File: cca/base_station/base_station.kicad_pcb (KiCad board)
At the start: 2 copper layers, 76.2 x 50.8 mm, 11 parts, among them P1 tstat_ui_conn, P2 tstat_cable_con, U1 RFM69W, U2 DHT22, U3 TEENSY-LC

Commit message: 0.5mm fab pass
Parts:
- moved AE1 6.54 mm to (34.5, 52.9)
- moved P2 2.54 mm to (88.1, 35.6)
- moved U1 2.54 mm to (56.1, 62.3)
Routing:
- net Net-(AE1-Pad1): track 7.89 -> 3.89 mm
- net +3V3: track 122.1 -> 126.0 mm, vias 3 -> 2
- net Net-(U1-Pad2): track 44.3 -> 47.9 mm
- net Net-(P2-Pad7): track 13.4 -> 10.9 mm
- net Net-(P2-Pad6): track 13.5 -> 10.9 mm
- net Net-(P2-Pad5): track 13.5 -> 10.9 mm
- net Net-(P2-Pad4): track 13.5 -> 10.9 mm
- net Net-(P2-Pad8): track 13.4 -> 11.0 mm
- net Net-(U1-Pad15): track 41.0 -> 39.0 mm
- net GND: track 24.1 -> 25.6 mm
- net Net-(P1-Pad5): track 21.1 -> 19.6 mm
- net Net-(P1-Pad3): track 19.1 -> 20.5 mm
- net Net-(U1-Pad13): track 35.3 -> 34.4 mm
- net Net-(U1-Pad14): track 38.0 -> 37.3 mm
- net +5V: track 78.1 -> 77.6 mm
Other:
- net class 3.3v: clearance 0.2 -> 0.51; via_dia 1.1 -> 1.5
- net class 5v: clearance 0.4 -> 0.51; via_dia 1.1 -> 1.5
- net class Default: clearance 0.4 -> 0.51; trace_width 0.25 -> 0.5; via_dia 1.1 -> 1.5
- net class ant: clearance 0.4 -> 0.51; via_dia 1.1 -> 1.5
- net class gnd: clearance 0.2 -> 0.51; via_dia 1.1 -> 1.5
- rule trace_clearance: 0.4 -> 0.51
- rule trace_min: 0.2 -> 0.5

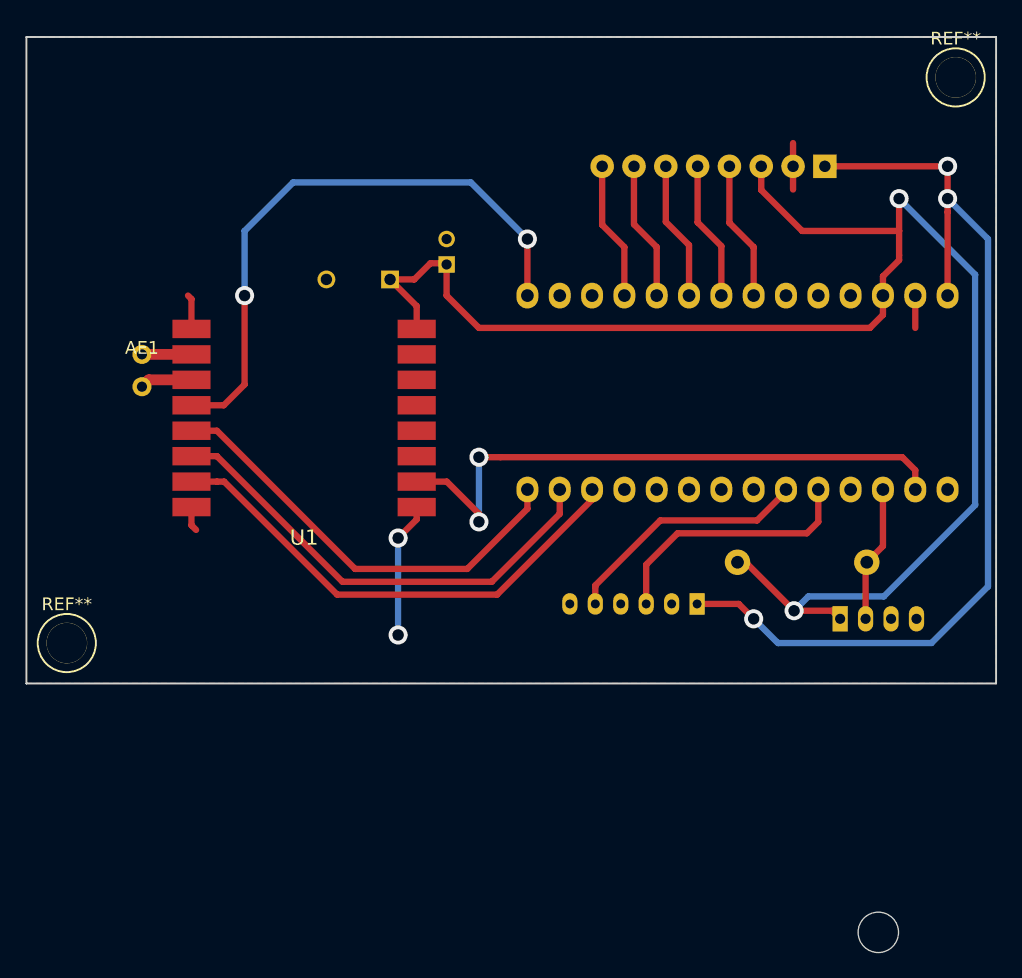
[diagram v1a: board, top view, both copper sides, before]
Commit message: updated wire holes and antenna to be 1.0mm drill. Added missing 3.3V optional e-point
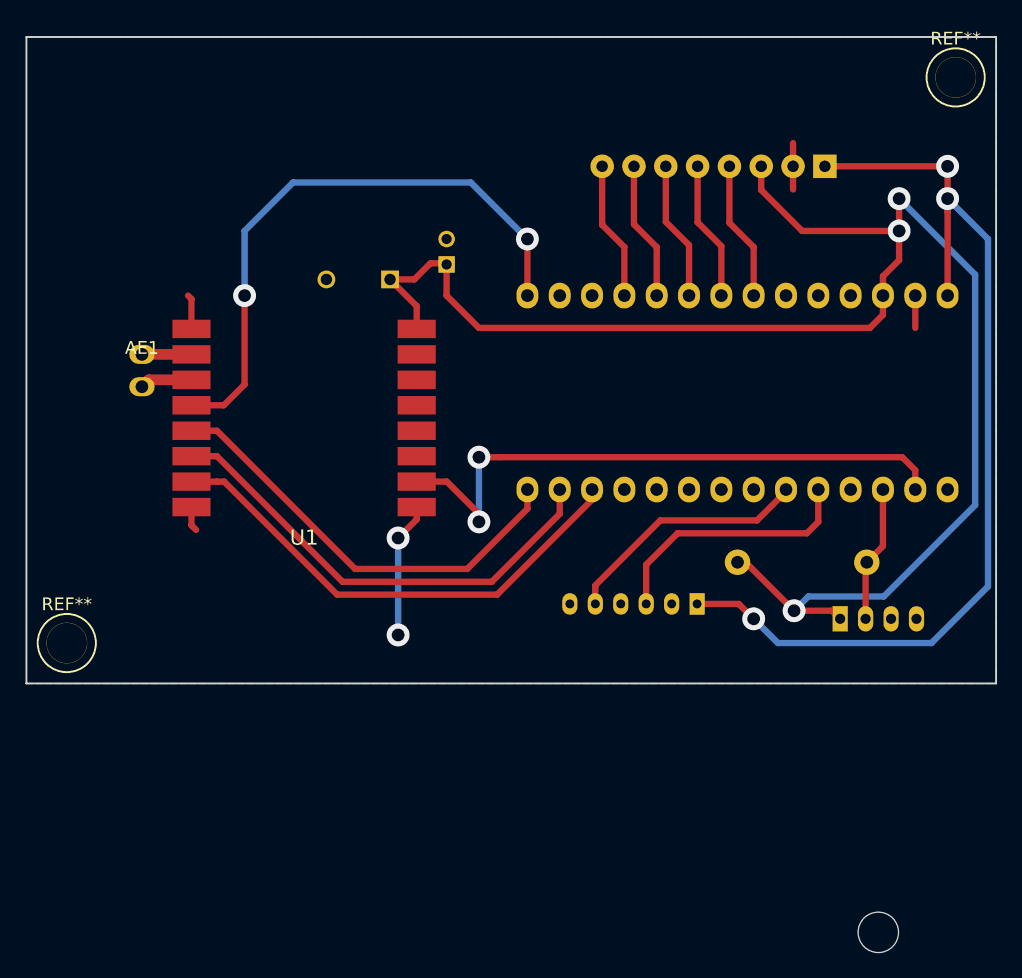
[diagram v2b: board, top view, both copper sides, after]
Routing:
- net +3V3: vias 2 -> 3
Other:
- net class 3.3v: via_dia 1.5 -> 1.8; via_drill 0.9 -> 1
- net class 5v: via_dia 1.5 -> 1.8; via_drill 0.9 -> 1
- net class Default: via_dia 1.5 -> 1.8; via_drill 0.9 -> 1
- net class ant: via_dia 1.5 -> 1.8; via_drill 0.9 -> 1
- net class gnd: via_dia 1.5 -> 1.8; via_drill 0.9 -> 1
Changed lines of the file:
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@@
     (links 36)
     (no_connects 0)
-    (area 25.324999 24.242 102.115 98.883001)
+    (area 25.324999 25.324999 101.675001 76.275001)
     (thickness 1.6)
     (drawings 4)
-    (tracks 128)
+    (tracks 129)
     (zones 0)
     (modules 11)
@@
     (segment_width 0.2)
     (edge_width 0.15)
-    (via_size 1.5)
-    (via_drill 0.9)
+    (via_size 1.8)
+    (via_drill 1)
     (via_min_size 0.4)
     (via_min_drill 0.3)
@@
     (clearance 0.51)
     (trace_width 0.5)
-    (via_dia 1.5)
-    (via_drill 0.9)
+    (via_dia 1.8)
+    (via_drill 1)
     (uvia_dia 0.3)
     (uvia_drill 0.1)
@@
     (clearance 0.51)
     (trace_width 0.5)
-    (via_dia 1.5)
-    (via_drill 0.9)
+    (via_dia 1.8)
+    (via_drill 1)
     (uvia_dia 0.3)
     (uvia_drill 0.1)
@@
     (clearance 0.51)
     (trace_width 0.5)
-    (via_dia 1.5)
-    (via_drill 0.9)
+    (via_dia 1.8)
+    (via_drill 1)
     (uvia_dia 0.3)
     (uvia_drill 0.1)
@@
     (clearance 0.51)
     (trace_width 0.85)
-    (via_dia 1.5)
-    (via_drill 0.9)
+    (via_dia 1.8)
+    (via_drill 1)
     (uvia_dia 0.3)
     (uvia_drill 0.1)
@@
     (clearance 0.51)
     (trace_width 0.5)
-    (via_dia 1.5)
-    (via_drill 0.9)
+    (via_dia 1.8)
+    (via_drill 1)
     (uvia_dia 0.3)
     (uvia_drill 0.1)
@@
     (pad 1 thru_hole circle (at 0 0) (size 3.2 3.2) (drill 3.175) (layers *.Cu *.Mask F.SilkS))
   )
-  (module t_footprints:ant_915_dipole_conn (layer F.Cu)
-    (at 34.48 52.88)
-    (descr "module 1 pin (ou trou mecanique de percage)")
-    (tags DEV)
-    (fp_text reference AE1 (at 0 -3.048) (layer F.SilkS)
-      (effects (font (size 1 1) (thickness 0.15)))
-    )
-    (fp_text value ANTENNA_915 (at 0 2.794) (layer F.Fab)
-      (effects (font (size 1 1) (thickness 0.15)))
-    )
-    (pad 1 thru_hole circle (at 0 -2.54) (size 1.5 1.5) (drill 0.8) (layers *.Cu *.Mask)
-      (net 9 "Net-(AE1-Pad1)"))
-    (pad 2 thru_hole circle (at 0 0) (size 1.5 1.5) (drill 0.8) (layers *.Cu *.Mask)
-      (net 2 GND))
-  )
   (module t_footprints:Resistor_Horizontal_RM10mm (layer B.Cu)
     (at 81.28 66.675)
@@
       (net 2 GND))
   )
+  (module t_footprints:ant_915_dipole_conn (layer F.Cu)
+    (at 34.48 52.88)
+    (descr "module 1 pin (ou trou mecanique de percage)")
+    (tags DEV)
+    (fp_text reference AE1 (at 0 -3.048) (layer F.SilkS)
+      (effects (font (size 1 1) (thickness 0.15)))
+    )
+    (fp_text value ANTENNA_915 (at 0 2.794) (layer F.Fab)
+      (effects (font (size 1 1) (thickness 0.15)))
+    )
+    (pad 1 thru_hole oval (at 0 -2.54) (size 2 1.5) (drill 1) (layers *.Cu *.Mask)
+      (net 9 "Net-(AE1-Pad1)"))
+    (pad 2 thru_hole oval (at 0 0) (size 2 1.5) (drill 1) (layers *.Cu *.Mask)
+      (net 2 GND))
+  )
   (gr_line (start 101.6 25.4) (end 25.4 25.4) (layer Edge.Cuts) (width 0.15))
   (gr_line (start 101.6 76.2) (end 101.6 25.4) (layer Edge.Cuts) (width 0.15))
   (gr_line (start 25.4 76.2) (end 101.6 76.2) (layer Edge.Cuts) (width 0.15))
   (gr_line (start 25.4 25.4) (end 25.4 76.2) (layer Edge.Cuts) (width 0.15))
+  (via (at 93.98 40.64) (size 1.8) (drill 1) (layers F.Cu B.Cu) (net 1))
   (segment (start 92.781666 69.35999) (end 86.85001 69.35999) (width 0.5) (layer B.Cu) (net 1))
   (segment (start 86.85001 69.35999) (end 85.725 70.485) (width 0.5) (layer B.Cu) (net 1))
-  (via (at 85.725 70.485) (size 1.5) (drill 0.9) (layers F.Cu B.Cu) (net 1))
+  (via (at 85.725 70.485) (size 1.8) (drill 1) (layers F.Cu B.Cu) (net 1))
   (segment (start 93.98 38.1) (end 99.95499 44.07499) (width 0.5) (layer B.Cu) (net 1))
   (segment (start 99.95499 44.07499) (end 99.95499 62.186666) (width 0.5) (layer B.Cu) (net 1))
@@
   (segment (start 83.145 37.425) (end 86.36 40.64) (width 0.5) (layer F.Cu) (net 1))
   (segment (start 93.98 40.64) (end 86.36 40.64) (width 0.5) (layer F.Cu) (net 1))
-  (via (at 93.98 38.1) (size 1.5) (drill 0.9) (layers F.Cu B.Cu) (net 1))
+  (via (at 93.98 38.1) (size 1.8) (drill 1) (layers F.Cu B.Cu) (net 1))
   (segment (start 93.98 42.545) (end 93.98 40.64) (width 0.5) (layer F.Cu) (net 1))
   (segment (start 93.98 42.934) (end 93.98 42.545) (width 0.5) (layer F.Cu) (net 1))
@@
   (segment (start 85.725 70.485) (end 88.71 70.485) (width 0.5) (layer F.Cu) (net 1))
   (segment (start 54.61 64.77) (end 54.61 72.39) (width 0.5) (layer B.Cu) (net 2))
-  (via (at 54.61 72.39) (size 1.5) (drill 0.9) (layers F.Cu B.Cu) (net 2))
+  (via (at 54.61 72.39) (size 1.8) (drill 1) (layers F.Cu B.Cu) (net 2))
   (segment (start 56.07 62.34) (end 56.07 63.31) (width 0.5) (layer F.Cu) (net 2))
   (segment (start 56.07 63.31) (end 54.61 64.77) (width 0.5) (layer F.Cu) (net 2))
-  (via (at 54.61 64.77) (size 1.5) (drill 0.9) (layers F.Cu B.Cu) (net 2))
+  (via (at 54.61 64.77) (size 1.8) (drill 1) (layers F.Cu B.Cu) (net 2))
   (segment (start 38.37 48.34) (end 38.37 45.99) (width 0.5) (layer F.Cu) (net 2))
   (segment (start 38.37 45.99) (end 38.1 45.72) (width 0.5) (layer F.Cu) (net 2))
@@
   (segment (start 62.65566 58.42) (end 60.96 58.42) (width 0.5) (layer F.Cu) (net 4))
   (segment (start 94.226 58.42) (end 62.65566 58.42) (width 0.5) (layer F.Cu) (net 4))
-  (via (at 60.96 63.5) (size 1.5) (drill 0.9) (layers F.Cu B.Cu) (net 4))
-  (via (at 60.96 58.42) (size 1.5) (drill 0.9) (layers F.Cu B.Cu) (net 4))
+  (via (at 60.96 63.5) (size 1.8) (drill 1) (layers F.Cu B.Cu) (net 4))
+  (via (at 60.96 58.42) (size 1.8) (drill 1) (layers F.Cu B.Cu) (net 4))
   (segment (start 56.07 60.34) (end 58.435 60.34) (width 0.5) (layer F.Cu) (net 4))
   (segment (start 60.96 62.865) (end 60.96 63.5) (width 0.5) (layer F.Cu) (net 4))
@@
   (segment (start 64.77 41.275) (end 60.325 36.83) (width 0.5) (layer B.Cu) (net 5))
   (segment (start 64.77 45.72) (end 64.77 41.275) (width 0.5) (layer F.Cu) (net 5) (status 10))
-  (via (at 64.77 41.275) (size 1.5) (drill 0.9) (layers F.Cu B.Cu) (net 5))
+  (via (at 64.77 41.275) (size 1.8) (drill 1) (layers F.Cu B.Cu) (net 5))
   (segment (start 40.91 54.34) (end 42.545 52.705) (width 0.5) (layer F.Cu) (net 5))
   (segment (start 42.545 52.705) (end 42.545 45.72) (width 0.5) (layer F.Cu) (net 5))
-  (via (at 42.545 45.72) (size 1.5) (drill 0.9) (layers F.Cu B.Cu) (net 5))
+  (via (at 42.545 45.72) (size 1.8) (drill 1) (layers F.Cu B.Cu) (net 5))
   (segment (start 40.91 54.34) (end 38.37 54.34) (width 0.5) (layer F.Cu) (net 5))
   (segment (start 42.545 40.64) (end 42.545 45.72) (width 0.5) (layer B.Cu) (net 5))
@@
   (segment (start 38.37 50.34) (end 34.48 50.34) (width 0.85) (layer F.Cu) (net 9))
   (segment (start 96.52 73.025) (end 84.455 73.025) (width 0.5) (layer B.Cu) (net 10))
-  (via (at 97.79 38.1) (size 1.5) (drill 0.9) (layers F.Cu B.Cu) (net 10))
+  (via (at 97.79 38.1) (size 1.8) (drill 1) (layers F.Cu B.Cu) (net 10))
   (segment (start 100.965 41.275) (end 97.79 38.1) (width 0.5) (layer B.Cu) (net 10))
-  (via (at 82.55 71.12) (size 1.5) (drill 0.9) (layers F.Cu B.Cu) (net 10))
+  (via (at 82.55 71.12) (size 1.8) (drill 1) (layers F.Cu B.Cu) (net 10))
   (segment (start 100.965 68.58) (end 100.965 41.275) (width 0.5) (layer B.Cu) (net 10))
   (segment (start 96.52 73.025) (end 100.965 68.58) (width 0.5) (layer B.Cu) (net 10))
@@
   (segment (start 97.79 35.56) (end 88.145 35.56) (width 0.5) (layer F.Cu) (net 10))
   (segment (start 97.79 38.1) (end 97.79 35.56) (width 0.5) (layer F.Cu) (net 10))
-  (via (at 97.79 35.56) (size 1.5) (drill 0.9) (layers F.Cu B.Cu) (net 10))
+  (via (at 97.79 35.56) (size 1.8) (drill 1) (layers F.Cu B.Cu) (net 10))
   (segment (start 97.79 38.1) (end 97.79 39.16066) (width 0.5) (layer F.Cu) (net 10))
   (segment (start 97.79 39.16066) (end 97.79 45.72) (width 0.5) (layer F.Cu) (net 10) (status 20))

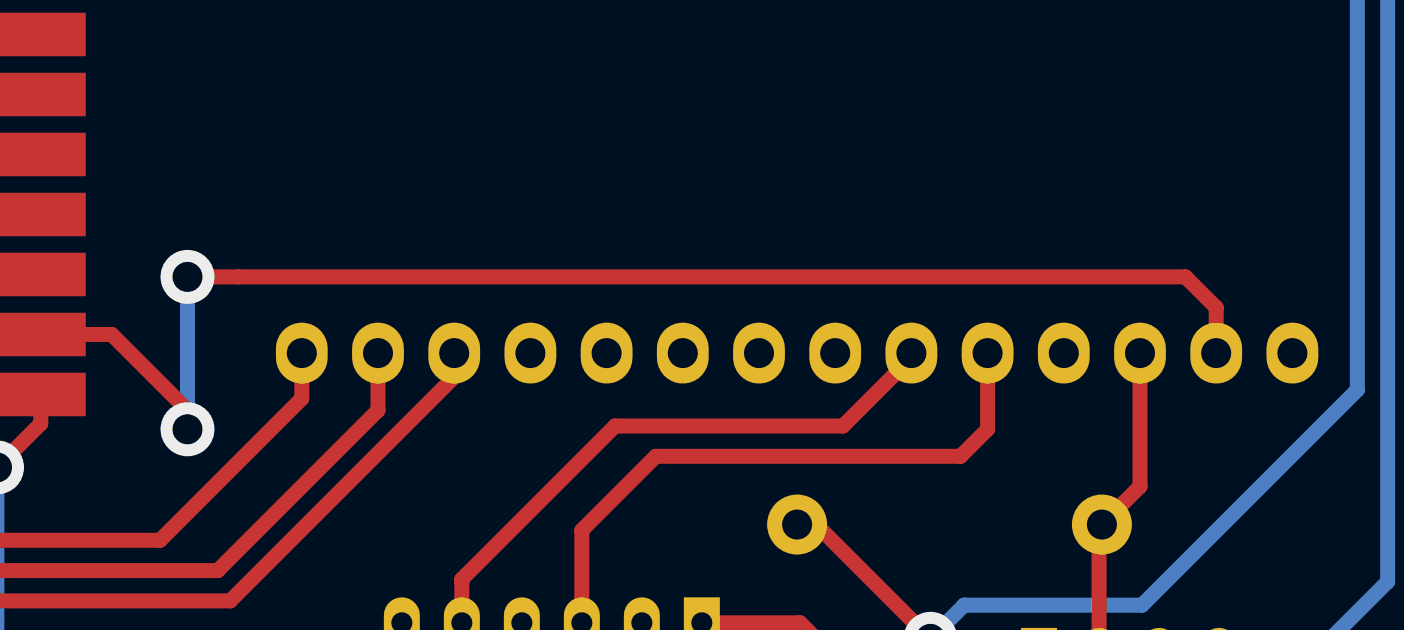
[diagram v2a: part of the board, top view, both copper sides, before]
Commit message: Moved rfm69w interrupt (dio0) to pin 2 of teensy-lc because pin 0 cannot function as an interrupt.
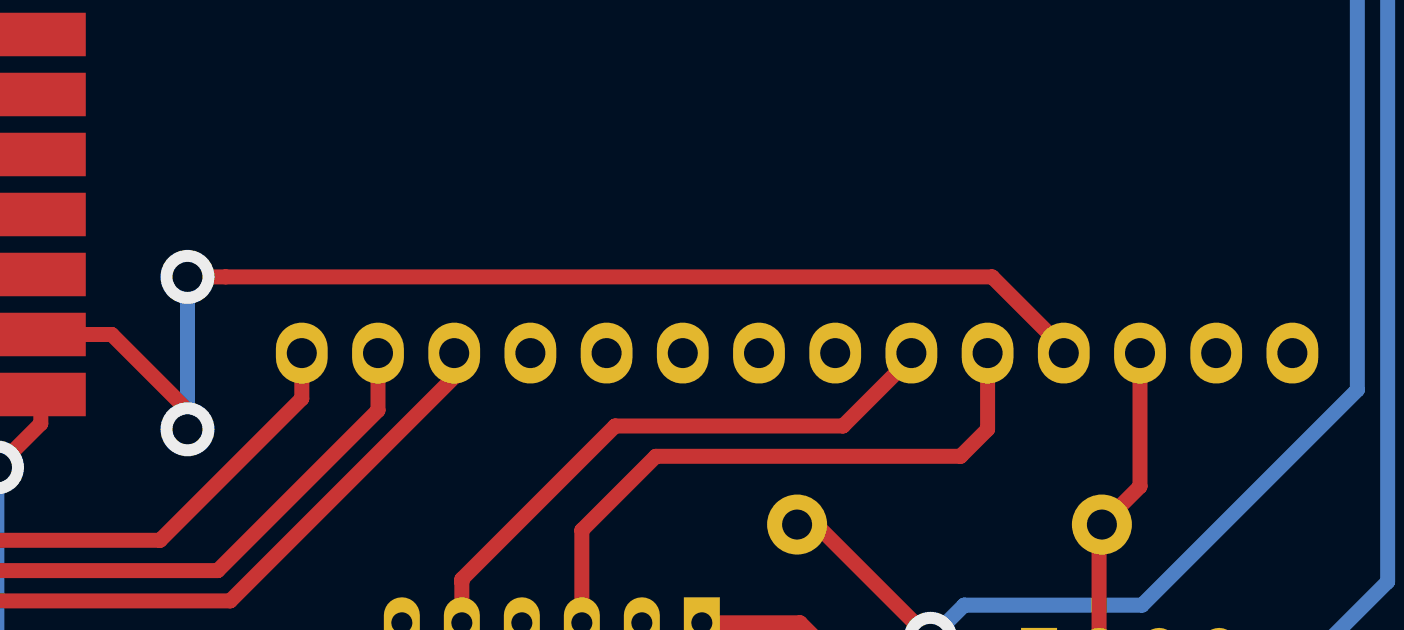
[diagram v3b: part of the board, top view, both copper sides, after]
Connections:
- U3 pad 0: Net-(U1-Pad2) -> (no net)
- U3 pad 2: (no net) -> Net-(U1-Pad2)
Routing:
- net Net-(U1-Pad2): track 47.9 -> 42.0 mm
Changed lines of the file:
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@@
     (links 36)
     (no_connects 0)
-    (area 25.324999 25.324999 101.675001 76.275001)
+    (area 25.324999 24.242 102.115 98.883001)
     (thickness 1.6)
     (drawings 4)
@@
     (fp_line (start 27.94 2.54) (end -2.54 2.54) (layer B.SilkS) (width 0.15))
     (fp_line (start -2.54 2.54) (end -2.54 12.7) (layer B.SilkS) (width 0.15))
-    (pad 0 thru_hole oval (at 0 0 180) (size 1.7272 2.032) (drill 1) (layers *.Cu *.Mask B.SilkS)
-      (net 4 "Net-(U1-Pad2)"))
+    (pad 0 thru_hole oval (at 0 0 180) (size 1.7272 2.032) (drill 1) (layers *.Cu *.Mask B.SilkS))
     (pad 1 thru_hole oval (at 2.54 0 180) (size 1.7272 2.032) (drill 1) (layers *.Cu *.Mask B.SilkS)
       (net 3 "Net-(R1-Pad2)"))
-    (pad 2 thru_hole oval (at 5.08 0 180) (size 1.7272 2.032) (drill 1) (layers *.Cu *.Mask B.SilkS))
+    (pad 2 thru_hole oval (at 5.08 0 180) (size 1.7272 2.032) (drill 1) (layers *.Cu *.Mask B.SilkS)
+      (net 4 "Net-(U1-Pad2)"))
     (pad 3 thru_hole oval (at 7.62 0 180) (size 1.7272 2.032) (drill 1) (layers *.Cu *.Mask B.SilkS)
       (net 11 "Net-(P1-Pad3)"))
@@
   (segment (start 92.71 60.96) (end 92.71 65.405) (width 0.5) (layer F.Cu) (net 3) (status 10))
   (segment (start 92.71 65.405) (end 91.44 66.675) (width 0.5) (layer F.Cu) (net 3))
+  (segment (start 90.17 60.96) (end 90.17 60.8076) (width 0.5) (layer F.Cu) (net 4))
+  (segment (start 62.232792 58.42) (end 60.96 58.42) (width 0.5) (layer F.Cu) (net 4))
+  (segment (start 90.17 60.8076) (end 87.7824 58.42) (width 0.5) (layer F.Cu) (net 4))
+  (segment (start 87.7824 58.42) (end 62.232792 58.42) (width 0.5) (layer F.Cu) (net 4))
   (segment (start 60.96 63.5) (end 60.96 58.42) (width 0.5) (layer B.Cu) (net 4))
-  (segment (start 95.25 59.444) (end 95.25 60.96) (width 0.5) (layer F.Cu) (net 4) (status 10))
-  (segment (start 95.25 59.444) (end 94.226 58.42) (width 0.5) (layer F.Cu) (net 4))
-  (segment (start 62.65566 58.42) (end 60.96 58.42) (width 0.5) (layer F.Cu) (net 4))
-  (segment (start 94.226 58.42) (end 62.65566 58.42) (width 0.5) (layer F.Cu) (net 4))
   (via (at 60.96 63.5) (size 1.8) (drill 1) (layers F.Cu B.Cu) (net 4))
   (via (at 60.96 58.42) (size 1.8) (drill 1) (layers F.Cu B.Cu) (net 4))
